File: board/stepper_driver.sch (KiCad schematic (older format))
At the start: 13 parts

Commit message: Wired up the stepper driver blocks in the main schematic.
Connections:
- new net: J?.~ (2B), U?.~ (~STBY/RST) (x3)
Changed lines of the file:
@@
 LIBS:contrib
 LIBS:valves
+LIBS:74xgxx
+LIBS:ac-dc
+LIBS:brooktre
+LIBS:cmos_ieee
+LIBS:dc-dc
+LIBS:elec-unifil
+LIBS:gennum
+LIBS:graphic
+LIBS:hc11
+LIBS:microchip1
+LIBS:microchip_pic10mcu
+LIBS:microchip_pic12mcu
+LIBS:microchip_pic16mcu
+LIBS:msp430
+LIBS:nxp_armmcu
+LIBS:powerint
+LIBS:pspice
+LIBS:sensors
+LIBS:transf
+LIBS:ttl_ieee
+LIBS:video
 LIBS:components
-LIBS:stepper_driver-cache
+LIBS:robot_controller-cache
 EELAYER 24 0
 EELAYER END
 $Descr USLetter 11000 8500
 encoding utf-8
-Sheet 1 1
+Sheet 3 5
 Title ""
 Date "21 jan 2014"
@@
 U 1 1 52E46BDA
 P 6900 4550
+AR Path="/52E6C2E8/52E46BDA" Ref="J?"  Part="1"
+AR Path="/52E72F84/52E46BDA" Ref="J?"  Part="1"
 F 0 "J?" H 6800 4200 60  0000 C CNN
 F 1 "CONN_STEPPER" V 7150 4550 60  0001 C CNN
@@
 U 1 1 52E46C46
 P 4450 3200
+AR Path="/52E6C2E8/52E46C46" Ref="#PWR01"  Part="1"
+AR Path="/52E72F84/52E46C46" Ref="#PWR01"  Part="1"
 F 0 "#PWR01" H 4450 3200 30  0001 C CNN
 F 1 "GND" H 4450 3130 30  0001 C CNN
@@
 U 1 1 52E46C5A
 P 4750 3200
+AR Path="/52E6C2E8/52E46C5A" Ref="#PWR02"  Part="1"
+AR Path="/52E72F84/52E46C5A" Ref="#PWR02"  Part="1"
 F 0 "#PWR02" H 4750 3200 30  0001 C CNN
 F 1 "GND" H 4750 3130 30  0001 C CNN
@@
 U 1 1 52E46C96
 P 4450 2600
+AR Path="/52E6C2E8/52E46C96" Ref="#PWR03"  Part="1"
+AR Path="/52E72F84/52E46C96" Ref="#PWR03"  Part="1"
 F 0 "#PWR03" H 4450 2560 30  0001 C CNN
 F 1 "+3.3V" H 4450 2710 30  0000 C CNN
@@
 U 1 1 52E46CA8
 P 4750 2600
+AR Path="/52E6C2E8/52E46CA8" Ref="#PWR04"  Part="1"
+AR Path="/52E72F84/52E46CA8" Ref="#PWR04"  Part="1"
 F 0 "#PWR04" H 4750 2560 30  0001 C CNN
 F 1 "+3.3V" H 4750 2710 30  0000 C CNN
@@
 U 1 1 52E46CC8
 P 5150 3150
+AR Path="/52E6C2E8/52E46CC8" Ref="#PWR05"  Part="1"
+AR Path="/52E72F84/52E46CC8" Ref="#PWR05"  Part="1"
 F 0 "#PWR05" H 5150 3110 30  0001 C CNN
 F 1 "+3.3V" H 5150 3260 30  0000 C CNN
@@
 U 1 1 52E46D7E
 P 5750 3150
+AR Path="/52E6C2E8/52E46D7E" Ref="#PWR06"  Part="1"
+AR Path="/52E72F84/52E46D7E" Ref="#PWR06"  Part="1"
 F 0 "#PWR06" H 5750 3100 20  0001 C CNN
 F 1 "+24V" H 5750 3250 30  0000 C CNN
@@
 U 1 1 52E46E0C
 P 6100 2350
+AR Path="/52E6C2E8/52E46E0C" Ref="D?"  Part="1"
+AR Path="/52E72F84/52E46E0C" Ref="D?"  Part="1"
 F 0 "D?" H 6100 2450 40  0000 C CNN
 F 1 "DIODE" H 6100 2250 40  0000 C CNN
@@
 U 1 1 52E46E92
 P 6350 2000
+AR Path="/52E6C2E8/52E46E92" Ref="#PWR07"  Part="1"
+AR Path="/52E72F84/52E46E92" Ref="#PWR07"  Part="1"
 F 0 "#PWR07" H 6350 1950 20  0001 C CNN
 F 1 "+24V" H 6350 2100 30  0000 C CNN
@@
 U 1 1 52E46DF0
 P 5500 2350
+AR Path="/52E6C2E8/52E46DF0" Ref="D?"  Part="1"
+AR Path="/52E72F84/52E46DF0" Ref="D?"  Part="1"
 F 0 "D?" H 5500 2450 40  0000 C CNN
 F 1 "DIODE" H 5500 2250 40  0000 C CNN
@@
 U 1 1 52E46FD2
 P 5450 5950
+AR Path="/52E6C2E8/52E46FD2" Ref="#PWR08"  Part="1"
+AR Path="/52E72F84/52E46FD2" Ref="#PWR08"  Part="1"
 F 0 "#PWR08" H 5450 5950 30  0001 C CNN
 F 1 "GND" H 5450 5880 30  0001 C CNN
@@
 U 1 1 52E47021
 P 6650 5350
+AR Path="/52E6C2E8/52E47021" Ref="#PWR09"  Part="1"
+AR Path="/52E72F84/52E47021" Ref="#PWR09"  Part="1"
 F 0 "#PWR09" H 6650 5350 30  0001 C CNN
 F 1 "GND" H 6650 5280 30  0001 C CNN
@@
 U 1 1 52E47051
 P 4450 5550
+AR Path="/52E6C2E8/52E47051" Ref="#PWR010"  Part="1"
+AR Path="/52E72F84/52E47051" Ref="#PWR010"  Part="1"
 F 0 "#PWR010" H 4450 5550 30  0001 C CNN
 F 1 "GND" H 4450 5480 30  0001 C CNN
@@
 U 1 1 52E4727D
 P 4000 5350
+AR Path="/52E6C2E8/52E4727D" Ref="P?"  Part="1"
+AR Path="/52E72F84/52E4727D" Ref="P?"  Part="1"
 F 0 "P?" V 3950 5350 40  0000 C CNN
 F 1 "CONN_2" V 4050 5350 40  0000 C CNN
@@
 U 1 1 52E475E9
 P 7500 3250
+AR Path="/52E6C2E8/52E475E9" Ref="R?"  Part="1"
+AR Path="/52E72F84/52E475E9" Ref="R?"  Part="1"
 F 0 "R?" V 7580 3250 40  0000 C CNN
 F 1 "16k" V 7507 3251 40  0000 C CNN
@@
 U 1 1 52E475F4
 P 7500 3500
+AR Path="/52E6C2E8/52E475F4" Ref="#PWR011"  Part="1"
+AR Path="/52E72F84/52E475F4" Ref="#PWR011"  Part="1"
 F 0 "#PWR011" H 7500 3500 30  0001 C CNN
 F 1 "GND" H 7500 3430 30  0001 C CNN
@@
 U 1 1 52E47672
 P 7500 2500
+AR Path="/52E6C2E8/52E47672" Ref="#PWR012"  Part="1"
+AR Path="/52E72F84/52E47672" Ref="#PWR012"  Part="1"
 F 0 "#PWR012" H 7500 2450 20  0001 C CNN
 F 1 "+24V" H 7500 2600 30  0000 C CNN
@@
 U 1 1 52E47703
 P 7500 2750
+AR Path="/52E6C2E8/52E47703" Ref="R?"  Part="1"
+AR Path="/52E72F84/52E47703" Ref="R?"  Part="1"
 F 0 "R?" V 7580 2750 40  0000 C CNN
 F 1 "1.1k" V 7507 2751 40  0000 C CNN
@@
 U 1 1 52E477BA
 P 6700 3200
+AR Path="/52E6C2E8/52E477BA" Ref="#PWR013"  Part="1"
+AR Path="/52E72F84/52E477BA" Ref="#PWR013"  Part="1"
 F 0 "#PWR013" H 6700 3200 30  0001 C CNN
 F 1 "GND" H 6700 3130 30  0001 C CNN
@@
 U 1 1 52E477C5
 P 7000 3200
+AR Path="/52E6C2E8/52E477C5" Ref="#PWR014"  Part="1"
+AR Path="/52E72F84/52E477C5" Ref="#PWR014"  Part="1"
 F 0 "#PWR014" H 7000 3200 30  0001 C CNN
 F 1 "GND" H 7000 3130 30  0001 C CNN
@@
 U 1 1 52E477D0
 P 6700 2600
+AR Path="/52E6C2E8/52E477D0" Ref="#PWR015"  Part="1"
+AR Path="/52E72F84/52E477D0" Ref="#PWR015"  Part="1"
 F 0 "#PWR015" H 6700 2550 20  0001 C CNN
 F 1 "+24V" H 6700 2700 30  0000 C CNN
@@
 U 1 1 52E477DB
 P 7000 2600
+AR Path="/52E6C2E8/52E477DB" Ref="#PWR016"  Part="1"
+AR Path="/52E72F84/52E477DB" Ref="#PWR016"  Part="1"
 F 0 "#PWR016" H 7000 2550 20  0001 C CNN
 F 1 "+24V" H 7000 2700 30  0000 C CNN
@@
 U 1 1 52E4789D
 P 4450 2900
+AR Path="/52E6C2E8/52E4789D" Ref="C?"  Part="1"
+AR Path="/52E72F84/52E4789D" Ref="C?"  Part="1"
 F 0 "C?" H 4450 3000 40  0000 L CNN
 F 1 "100nF" H 4456 2815 40  0000 L CNN
@@
 U 1 1 52E478B3
 P 6700 2900
+AR Path="/52E6C2E8/52E478B3" Ref="C?"  Part="1"
+AR Path="/52E72F84/52E478B3" Ref="C?"  Part="1"
 F 0 "C?" H 6700 3000 40  0000 L CNN
 F 1 "220nF" H 6706 2815 40  0000 L CNN
@@
 U 1 1 52E478C4
 P 7000 2900
+AR Path="/52E6C2E8/52E478C4" Ref="C?"  Part="1"
+AR Path="/52E72F84/52E478C4" Ref="C?"  Part="1"
 F 0 "C?" H 7050 3000 50  0000 L CNN
 F 1 "100uF" H 7050 2800 50  0000 L CNN
@@
 U 1 1 52E47A96
 P 4750 2900
+AR Path="/52E6C2E8/52E47A96" Ref="C?"  Part="1"
+AR Path="/52E72F84/52E47A96" Ref="C?"  Part="1"
 F 0 "C?" H 4800 3000 50  0000 L CNN
 F 1 "10uF" H 4800 2800 50  0000 L CNN
@@
 U 1 1 52E47AD8
 P 5800 2100
+AR Path="/52E6C2E8/52E47AD8" Ref="C?"  Part="1"
+AR Path="/52E72F84/52E47AD8" Ref="C?"  Part="1"
 F 0 "C?" H 5800 2200 40  0000 L CNN
 F 1 "220nF" H 5806 2015 40  0000 L CNN
@@
 U 1 1 52E47AE3
 P 5500 2700
+AR Path="/52E6C2E8/52E47AE3" Ref="C?"  Part="1"
+AR Path="/52E72F84/52E47AE3" Ref="C?"  Part="1"
 F 0 "C?" H 5500 2800 40  0000 L CNN
 F 1 "10nF" H 5506 2615 40  0000 L CNN
@@
 U 1 1 52E6B5EE
 P 5500 4550
+AR Path="/52E6C2E8/52E6B5EE" Ref="U?"  Part="1"
+AR Path="/52E72F84/52E6B5EE" Ref="U?"  Part="1"
 F 0 "U?" H 4850 3600 60  0000 C CNN
 F 1 "L6470" H 5500 4550 60  0000 C CNN

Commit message: Wired up the stepper driver blocks in the main schematic. Titled the sheets.
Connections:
- new net: J?.~ (2B), U?.~ (~STBY/RST) (x3)
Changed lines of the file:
@@
 $Descr USLetter 11000 8500
 encoding utf-8
-Sheet 3 5
-Title ""
+Sheet 2 9
+Title "L64470 Stepper Driver"
 Date "21 jan 2014"
 Rev ""

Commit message: FTDI USB
I have added USB connectivity to this processor via an FT232RL
interface chip.
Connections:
- new net: J?.~ (2B), U?.~ (~STBY/RST) (x3)
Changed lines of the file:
@@
 LIBS:intel
 LIBS:audio
-LIBS:interface
 LIBS:digital-audio
 LIBS:philips

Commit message: SPI for Steppers and Temperature
I cleaned up the stepper driver section of the main schematic and
routed the high speed SPI interface over to it. I also got the second
SPI module connected to the temperature sensors.
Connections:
- new net: J?.~ (2B), U?.~ (~STBY/RST) (x3)
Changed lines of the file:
@@
 $Descr USLetter 11000 8500
 encoding utf-8
-Sheet 2 9
+Sheet 2 7
 Title "L64470 Stepper Driver"
 Date "21 jan 2014"

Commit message: Added the LED data lines and connector
I have added the LED data lines to the main schematic along with the
connector.
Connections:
- new net: J?.~ (2B), U?.~ (~STBY/RST) (x3)
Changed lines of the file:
@@
 $Descr USLetter 11000 8500
 encoding utf-8
-Sheet 2 7
+Sheet 2 8
 Title "L64470 Stepper Driver"
 Date "21 jan 2014"

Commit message: Schematic Additions
* UEXT
* AUX UART
* Regulator
* Fixed hirearchical label directions
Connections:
- new net: J?.~ (2B), U?.~ (~STBY/RST) (x3)
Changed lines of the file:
@@
 $Descr USLetter 11000 8500
 encoding utf-8
-Sheet 2 8
+Sheet 2 10
 Title "L64470 Stepper Driver"
 Date "21 jan 2014"

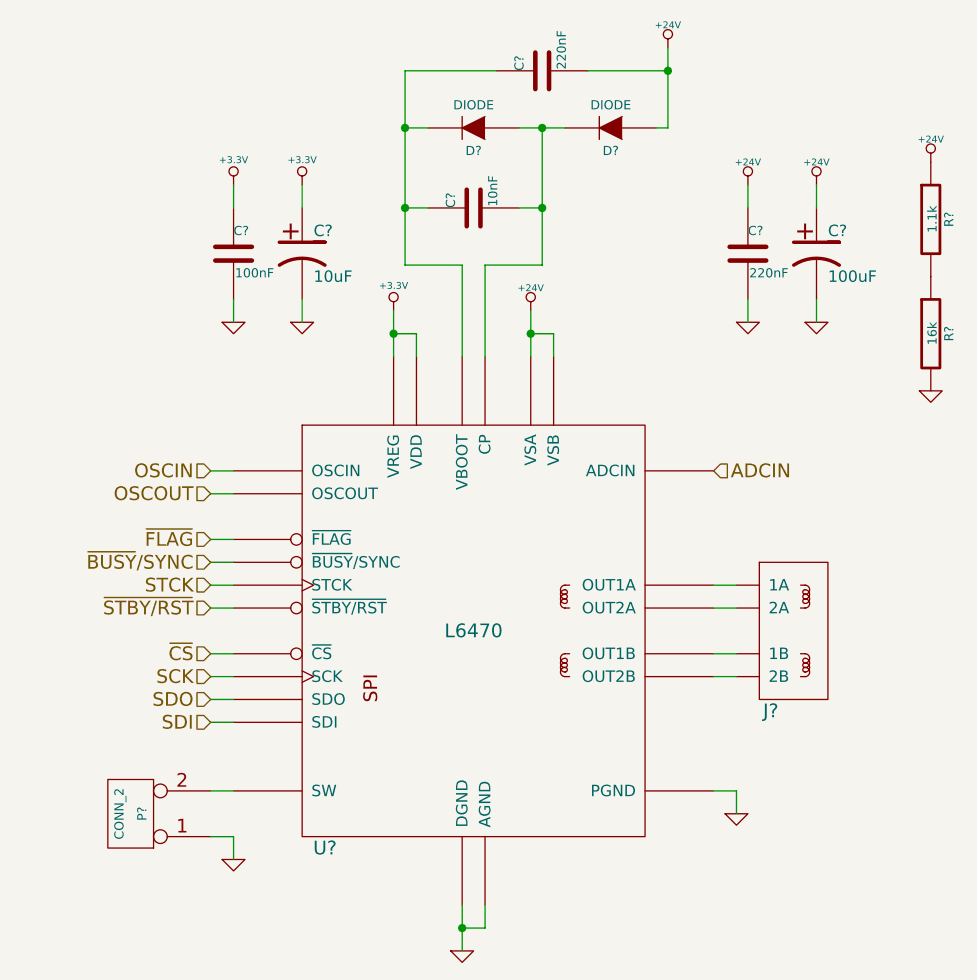
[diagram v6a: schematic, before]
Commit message: Replaces the 2 diodes with a double shottky diode for the steppers.
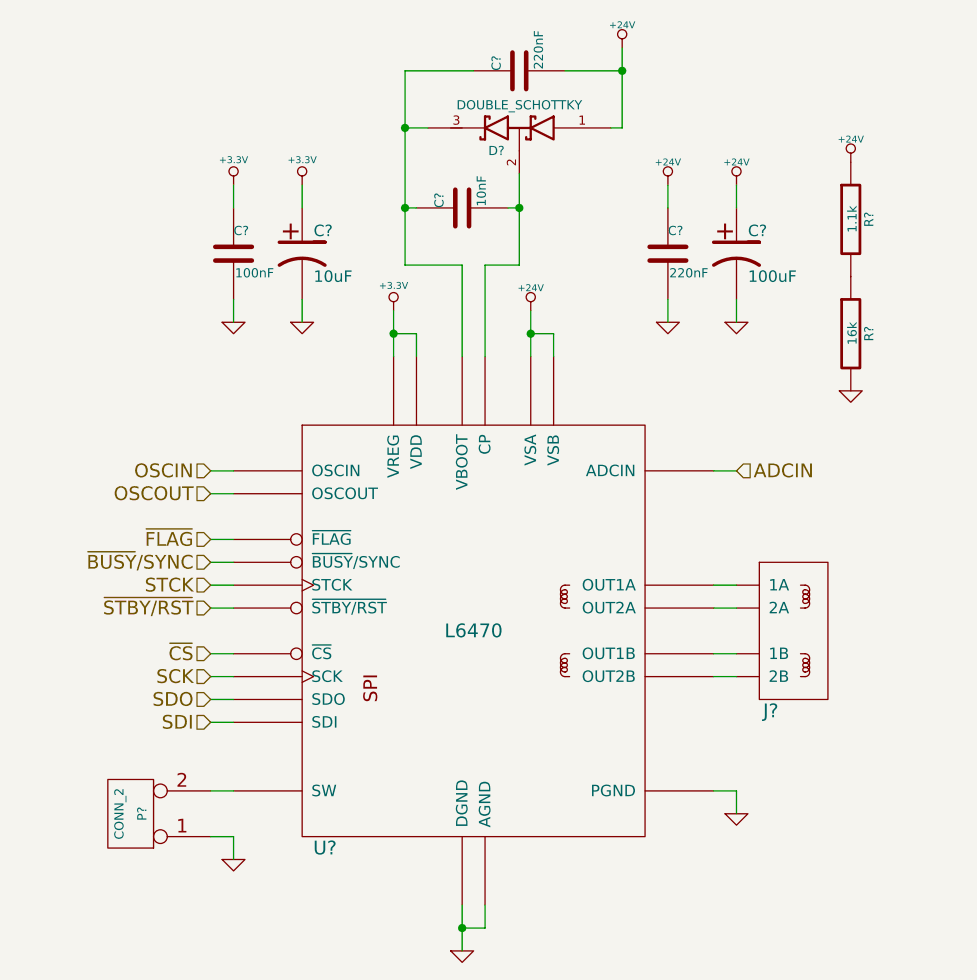
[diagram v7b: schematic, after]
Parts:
- removed D? (x2): DIODE, symbol DIODE
- added D?: DOUBLE_SCHOTTKY, symbol DOUBLE_SCHOTTKY
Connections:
- net +24V: now also D?.1 (Anode)
- net at C?.2, U?.~ (~STBY/RST): now also D?.2 (AK)
- net at C?.1, C?.1, U?.~ (~STBY/RST): now also D?.3 (cathode)
- new net: J?.~ (2B), U?.~ (~STBY/RST) (x3)
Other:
- moved on the sheet: C?, R?
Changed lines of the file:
@@
-$EndComp
-$Comp
-L DIODE D?
-U 1 1 52E46E0C
-P 6100 2350
-AR Path="/52E6C2E8/52E46E0C" Ref="D?"  Part="1"
-AR Path="/52E72F84/52E46E0C" Ref="D?"  Part="1"
-F 0 "D?" H 6100 2450 40  0000 C CNN
-F 1 "DIODE" H 6100 2250 40  0000 C CNN
-F 2 "" H 6100 2350 60  0000 C CNN
-F 3 "" H 6100 2350 60  0000 C CNN
-	1    6100 2350
-	-1   0    0    1
 $EndComp
 $Comp
 L +24V #PWR07
 U 1 1 52E46E92
-P 6350 2000
+P 6150 2000
 AR Path="/52E6C2E8/52E46E92" Ref="#PWR07"  Part="1"
 AR Path="/52E72F84/52E46E92" Ref="#PWR07"  Part="1"
-F 0 "#PWR07" H 6350 1950 20  0001 C CNN
-F 1 "+24V" H 6350 2100 30  0000 C CNN
-F 2 "" H 6350 2000 60  0000 C CNN
-F 3 "" H 6350 2000 60  0000 C CNN
-	1    6350 2000
-	1    0    0    -1
-$EndComp
-$Comp
-L DIODE D?
-U 1 1 52E46DF0
-P 5500 2350
-AR Path="/52E6C2E8/52E46DF0" Ref="D?"  Part="1"
-AR Path="/52E72F84/52E46DF0" Ref="D?"  Part="1"
-F 0 "D?" H 5500 2450 40  0000 C CNN
-F 1 "DIODE" H 5500 2250 40  0000 C CNN
-F 2 "" H 5500 2350 60  0000 C CNN
-F 3 "" H 5500 2350 60  0000 C CNN
-	1    5500 2350
-	-1   0    0    1
+F 0 "#PWR07" H 6150 1950 20  0001 C CNN
+F 1 "+24V" H 6150 2100 30  0000 C CNN
+F 2 "" H 6150 2000 60  0000 C CNN
+F 3 "" H 6150 2000 60  0000 C CNN
+	1    6150 2000
+	1    0    0    -1
 $EndComp
 Wire Wire Line
@@
 Connection ~ 5750 3250
 Wire Wire Line
-	5700 2350 5900 2350
-Wire Wire Line
-	5800 2350 5800 2950
-Connection ~ 5800 2350
-Wire Wire Line
-	5200 2700 5300 2700
+	5200 2700 5250 2700
 Wire Wire Line
 	5300 2350 5200 2350
 Connection ~ 5200 2350
-Wire Wire Line
-	5700 2700 5800 2700
 Connection ~ 5200 2700
-Connection ~ 5800 2700
-Connection ~ 6350 2100
-Wire Wire Line
-	6350 2350 6300 2350
-Wire Wire Line
-	6350 2000 6350 2350
-Wire Wire Line
-	6000 2100 6350 2100
+Connection ~ 6150 2100
+Wire Wire Line
+	6150 2350 6100 2350
+Wire Wire Line
+	6150 2000 6150 2350
+Wire Wire Line
+	5900 2100 6150 2100
 Wire Wire Line
 	5200 2100 5200 2950
 Wire Wire Line
-	5200 2100 5600 2100
-Wire Wire Line
-	5200 2950 5450 2950
+	5200 2100 5500 2100
 Wire Wire Line
 	5450 2950 5450 3350
-Wire Wire Line
-	5800 2950 5550 2950
 Wire Wire Line
 	5550 2950 5550 3350
@@
 L R R?
 U 1 1 52E475E9
-P 7500 3250
+P 7150 3250
 AR Path="/52E6C2E8/52E475E9" Ref="R?"  Part="1"
 AR Path="/52E72F84/52E475E9" Ref="R?"  Part="1"
-F 0 "R?" V 7580 3250 40  0000 C CNN
-F 1 "16k" V 7507 3251 40  0000 C CNN
-F 2 "" V 7430 3250 30  0000 C CNN
-F 3 "" H 7500 3250 30  0000 C CNN
-	1    7500 3250
+F 0 "R?" V 7230 3250 40  0000 C CNN
+F 1 "16k" V 7157 3251 40  0000 C CNN
+F 2 "" V 7080 3250 30  0000 C CNN
+F 3 "" H 7150 3250 30  0000 C CNN
+	1    7150 3250
 	1    0    0    -1
 $EndComp
@@
 L GND #PWR011
 U 1 1 52E475F4
-P 7500 3500
+P 7150 3500
 AR Path="/52E6C2E8/52E475F4" Ref="#PWR011"  Part="1"
 AR Path="/52E72F84/52E475F4" Ref="#PWR011"  Part="1"
-F 0 "#PWR011" H 7500 3500 30  0001 C CNN
-F 1 "GND" H 7500 3430 30  0001 C CNN
-F 2 "" H 7500 3500 60  0000 C CNN
-F 3 "" H 7500 3500 60  0000 C CNN
-	1    7500 3500
+F 0 "#PWR011" H 7150 3500 30  0001 C CNN
+F 1 "GND" H 7150 3430 30  0001 C CNN
+F 2 "" H 7150 3500 60  0000 C CNN
+F 3 "" H 7150 3500 60  0000 C CNN
+	1    7150 3500
 	1    0    0    -1
 $EndComp
@@
 L +24V #PWR012
 U 1 1 52E47672
-P 7500 2500
+P 7150 2500
 AR Path="/52E6C2E8/52E47672" Ref="#PWR012"  Part="1"
 AR Path="/52E72F84/52E47672" Ref="#PWR012"  Part="1"
-F 0 "#PWR012" H 7500 2450 20  0001 C CNN
-F 1 "+24V" H 7500 2600 30  0000 C CNN
-F 2 "" H 7500 2500 60  0000 C CNN
-F 3 "" H 7500 2500 60  0000 C CNN
-	1    7500 2500
+F 0 "#PWR012" H 7150 2450 20  0001 C CNN
+F 1 "+24V" H 7150 2600 30  0000 C CNN
+F 2 "" H 7150 2500 60  0000 C CNN
+F 3 "" H 7150 2500 60  0000 C CNN
+	1    7150 2500
 	1    0    0    -1
 $EndComp
@@
 L R R?
 U 1 1 52E47703
-P 7500 2750
+P 7150 2750
 AR Path="/52E6C2E8/52E47703" Ref="R?"  Part="1"
 AR Path="/52E72F84/52E47703" Ref="R?"  Part="1"
-F 0 "R?" V 7580 2750 40  0000 C CNN
-F 1 "1.1k" V 7507 2751 40  0000 C CNN
-F 2 "" V 7430 2750 30  0000 C CNN
-F 3 "" H 7500 2750 30  0000 C CNN
-	1    7500 2750
-	1    0    0    -1
-$EndComp
-Text HLabel 6550 3850 2    60   Input ~ 0
+F 0 "R?" V 7230 2750 40  0000 C CNN
+F 1 "1.1k" V 7157 2751 40  0000 C CNN
+F 2 "" V 7080 2750 30  0000 C CNN
+F 3 "" H 7150 2750 30  0000 C CNN
+	1    7150 2750
+	1    0    0    -1
+$EndComp
+Text HLabel 6650 3850 2    60   Input ~ 0
 ADCIN
 $Comp
 L GND #PWR013
 U 1 1 52E477BA
-P 6700 3200
+P 6350 3200
 AR Path="/52E6C2E8/52E477BA" Ref="#PWR013"  Part="1"
 AR Path="/52E72F84/52E477BA" Ref="#PWR013"  Part="1"
-F 0 "#PWR013" H 6700 3200 30  0001 C CNN
-F 1 "GND" H 6700 3130 30  0001 C CNN
-F 2 "" H 6700 3200 60  0000 C CNN
-F 3 "" H 6700 3200 60  0000 C CNN
-	1    6700 3200
+F 0 "#PWR013" H 6350 3200 30  0001 C CNN
+F 1 "GND" H 6350 3130 30  0001 C CNN
+F 2 "" H 6350 3200 60  0000 C CNN
+F 3 "" H 6350 3200 60  0000 C CNN
+	1    6350 3200
 	1    0    0    -1
 $EndComp
@@
 L GND #PWR014
 U 1 1 52E477C5
-P 7000 3200
+P 6650 3200
 AR Path="/52E6C2E8/52E477C5" Ref="#PWR014"  Part="1"
 AR Path="/52E72F84/52E477C5" Ref="#PWR014"  Part="1"
-F 0 "#PWR014" H 7000 3200 30  0001 C CNN
-F 1 "GND" H 7000 3130 30  0001 C CNN
-F 2 "" H 7000 3200 60  0000 C CNN
-F 3 "" H 7000 3200 60  0000 C CNN
-	1    7000 3200
+F 0 "#PWR014" H 6650 3200 30  0001 C CNN
+F 1 "GND" H 6650 3130 30  0001 C CNN
+F 2 "" H 6650 3200 60  0000 C CNN
+F 3 "" H 6650 3200 60  0000 C CNN
+	1    6650 3200
 	1    0    0    -1
 $EndComp
@@
 L +24V #PWR015
 U 1 1 52E477D0
-P 6700 2600
+P 6350 2600
 AR Path="/52E6C2E8/52E477D0" Ref="#PWR015"  Part="1"
 AR Path="/52E72F84/52E477D0" Ref="#PWR015"  Part="1"
-F 0 "#PWR015" H 6700 2550 20  0001 C CNN
-F 1 "+24V" H 6700 2700 30  0000 C CNN
-F 2 "" H 6700 2600 60  0000 C CNN
-F 3 "" H 6700 2600 60  0000 C CNN
-	1    6700 2600
+F 0 "#PWR015" H 6350 2550 20  0001 C CNN
+F 1 "+24V" H 6350 2700 30  0000 C CNN
+F 2 "" H 6350 2600 60  0000 C CNN
+F 3 "" H 6350 2600 60  0000 C CNN
+	1    6350 2600
 	1    0    0    -1
 $EndComp
@@
 L +24V #PWR016
 U 1 1 52E477DB
-P 7000 2600
+P 6650 2600
 AR Path="/52E6C2E8/52E477DB" Ref="#PWR016"  Part="1"
 AR Path="/52E72F84/52E477DB" Ref="#PWR016"  Part="1"
-F 0 "#PWR016" H 7000 2550 20  0001 C CNN
-F 1 "+24V" H 7000 2700 30  0000 C CNN
-F 2 "" H 7000 2600 60  0000 C CNN
-F 3 "" H 7000 2600 60  0000 C CNN
-	1    7000 2600
+F 0 "#PWR016" H 6650 2550 20  0001 C CNN
+F 1 "+24V" H 6650 2700 30  0000 C CNN
+F 2 "" H 6650 2600 60  0000 C CNN
+F 3 "" H 6650 2600 60  0000 C CNN
+	1    6650 2600
 	1    0    0    -1
 $EndComp
@@
 L C C?
 U 1 1 52E478B3
-P 6700 2900
+P 6350 2900
 AR Path="/52E6C2E8/52E478B3" Ref="C?"  Part="1"
 AR Path="/52E72F84/52E478B3" Ref="C?"  Part="1"
-F 0 "C?" H 6700 3000 40  0000 L CNN
-F 1 "220nF" H 6706 2815 40  0000 L CNN
-F 2 "" H 6738 2750 30  0000 C CNN
-F 3 "" H 6700 2900 60  0000 C CNN
-	1    6700 2900
+F 0 "C?" H 6350 3000 40  0000 L CNN
+F 1 "220nF" H 6356 2815 40  0000 L CNN
+F 2 "" H 6388 2750 30  0000 C CNN
+F 3 "" H 6350 2900 60  0000 C CNN
+	1    6350 2900
 	1    0    0    -1
 $EndComp
@@
 L CP1 C?
 U 1 1 52E478C4
-P 7000 2900
+P 6650 2900
 AR Path="/52E6C2E8/52E478C4" Ref="C?"  Part="1"
 AR Path="/52E72F84/52E478C4" Ref="C?"  Part="1"
-F 0 "C?" H 7050 3000 50  0000 L CNN
-F 1 "100uF" H 7050 2800 50  0000 L CNN
-F 2 "" H 7000 2900 60  0000 C CNN
-F 3 "" H 7000 2900 60  0000 C CNN
-	1    7000 2900
-	1    0    0    -1
-$EndComp
-Wire Wire Line
-	6700 2600 6700 2700
-Wire Wire Line
-	6700 3100 6700 3200
-Wire Wire Line
-	7000 3100 7000 3200
-Wire Wire Line
-	7000 2700 7000 2600
+F 0 "C?" H 6700 3000 50  0000 L CNN
+F 1 "100uF" H 6700 2800 50  0000 L CNN
+F 2 "" H 6650 2900 60  0000 C CNN
+F 3 "" H 6650 2900 60  0000 C CNN
+	1    6650 2900
+	1    0    0    -1
+$EndComp
+Wire Wire Line
+	6350 2600 6350 2700
+Wire Wire Line
+	6350 3100 6350 3200
+Wire Wire Line
+	6650 3100 6650 3200
+Wire Wire Line
+	6650 2700 6650 2600
 Wire Wire Line
 	4450 3100 4450 3200
@@
 L C C?
 U 1 1 52E47AD8
-P 5800 2100
+P 5700 2100
 AR Path="/52E6C2E8/52E47AD8" Ref="C?"  Part="1"
 AR Path="/52E72F84/52E47AD8" Ref="C?"  Part="1"
-F 0 "C?" H 5800 2200 40  0000 L CNN
-F 1 "220nF" H 5806 2015 40  0000 L CNN
-F 2 "" H 5838 1950 30  0000 C CNN
-F 3 "" H 5800 2100 60  0000 C CNN
-	1    5800 2100
+F 0 "C?" H 5700 2200 40  0000 L CNN
+F 1 "220nF" H 5706 2015 40  0000 L CNN
+F 2 "" H 5738 1950 30  0000 C CNN
+F 3 "" H 5700 2100 60  0000 C CNN
+	1    5700 2100
 	0    -1   -1   0
 $EndComp
@@
 L C C?
 U 1 1 52E47AE3
-P 5500 2700
+P 5450 2700
 AR Path="/52E6C2E8/52E47AE3" Ref="C?"  Part="1"
 AR Path="/52E72F84/52E47AE3" Ref="C?"  Part="1"
-F 0 "C?" H 5500 2800 40  0000 L CNN
-F 1 "10nF" H 5506 2615 40  0000 L CNN
-F 2 "" H 5538 2550 30  0000 C CNN
-F 3 "" H 5500 2700 60  0000 C CNN
-	1    5500 2700
+F 0 "C?" H 5450 2800 40  0000 L CNN
+F 1 "10nF" H 5456 2615 40  0000 L CNN
+F 2 "" H 5488 2550 30  0000 C CNN
+F 3 "" H 5450 2700 60  0000 C CNN
+	1    5450 2700
 	0    -1   -1   0
 $EndComp
@@
 	1    0    0    -1
 $EndComp
+$Comp
+L DOUBLE_SCHOTTKY D?
+U 1 1 52F6EE9F
+P 5700 2350
+F 0 "D?" H 5800 2250 40  0000 C CNN
+F 1 "DOUBLE_SCHOTTKY" H 5700 2450 40  0000 C CNN
+F 2 "" H 5700 2350 60  0000 C CNN
+F 3 "" H 5700 2350 60  0000 C CNN
+	1    5700 2350
+	-1   0    0    -1
+$EndComp
+Wire Wire Line
+	5700 2550 5700 2950
+Wire Wire Line
+	5650 2700 5700 2700
+Connection ~ 5700 2700
+Wire Wire Line
+	5200 2950 5450 2950
+Wire Wire Line
+	5700 2950 5550 2950
+Wire Wire Line
+	6550 3850 6650 3850
 $EndSCHEMATC
